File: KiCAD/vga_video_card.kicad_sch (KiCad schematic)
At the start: 16 parts, among them J1 DE15_Socket_HighDensity, J6 Conn_02x16_Odd_Even, SW1 rst_btn, SW2 SW_DPDT_x2, SW3 SW_DPDT_x2, SW4 SW_DPDT_x2, U27 74HC04, U39 74HC02, Y1 10MHz

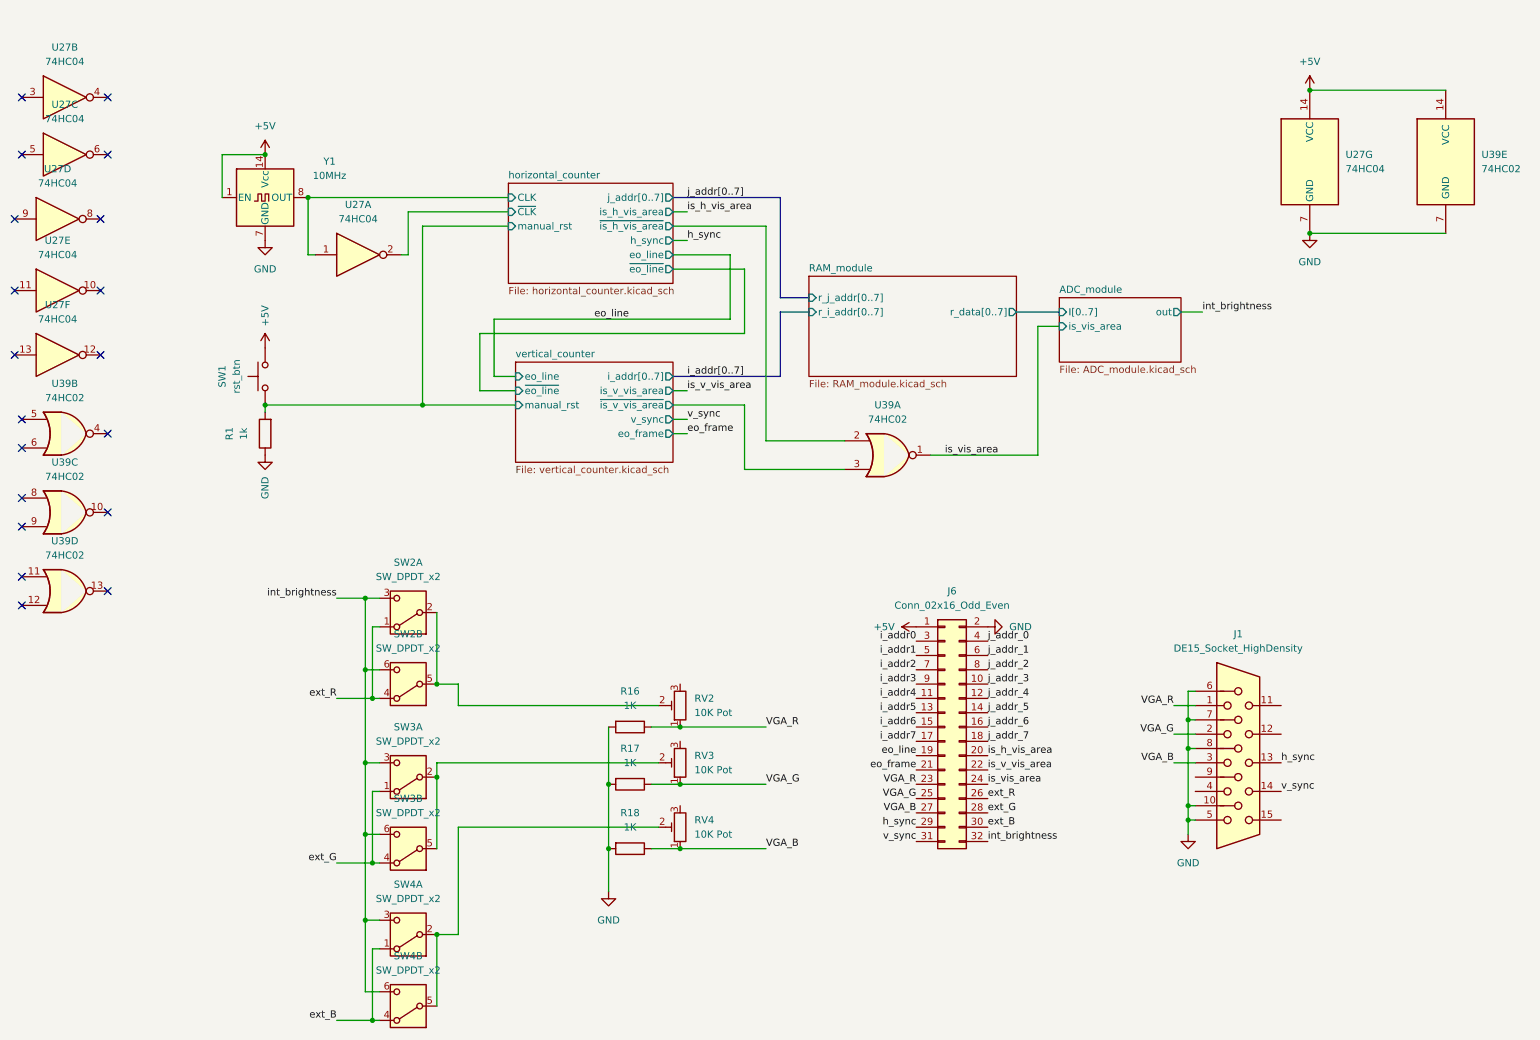
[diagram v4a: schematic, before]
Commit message: modified debug connector; changed board type in pcb editor
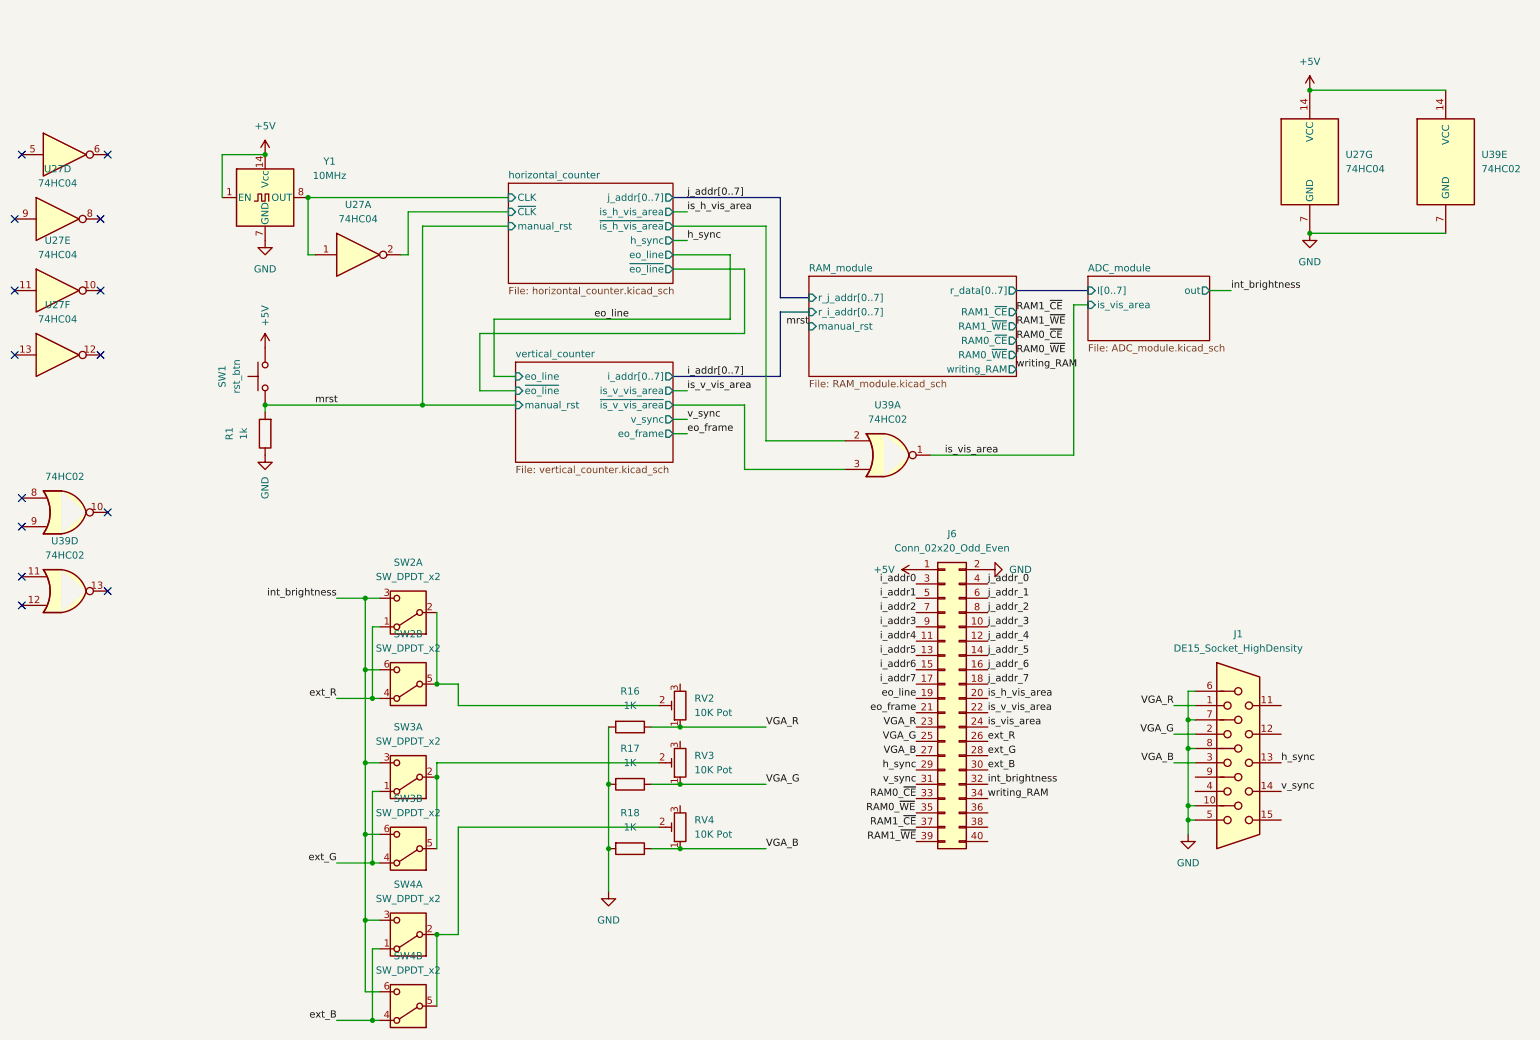
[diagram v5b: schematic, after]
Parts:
- removed J6: Conn_02x16_Odd_Even, Connector_PinSocket_2.54mm:PinSocket_2x16_P2.54mm_Vertical, symbol Connector_Generic:Conn_02x16_Odd_Even
- removed unit 2 of U27
- removed unit 2 of U39
- added J6: Conn_02x20_Odd_Even, Connector_PinSocket_2.54mm:PinSocket_2x20_P2.54mm_Vertical, symbol Connector_Generic:Conn_02x20_Odd_Even
- J1: footprint Connector_Dsub:DSUB-15_Socket_EdgeMount_P2.77mm -> Connector_Dsub:DSUB-15-HD_Socket_Horizontal_P2.29x1.90mm_EdgePinOffset3.03mm_Housed_MountingHolesOffset4.94mm
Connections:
- net +5V: now also J6.1 (Pin_1)
- net GND: now also J6.2 (Pin_2)
- net VGA_B: now also J6.27 (Pin_27)
- net VGA_G: now also J6.25 (Pin_25)
- net VGA_R: now also J6.23 (Pin_23)
- net eo_frame: now also J6.21 (Pin_21)
- net eo_line: now also J6.19 (Pin_19)
- net ext_B: now also J6.30 (Pin_30)
- net ext_G: now also J6.28 (Pin_28)
- net ext_R: now also J6.26 (Pin_26)
- net h_sync: now also J6.29 (Pin_29)
- net i_addr0: now also J6.3 (Pin_3)
- net i_addr1: now also J6.5 (Pin_5)
- net i_addr2: now also J6.7 (Pin_7)
- net i_addr3: now also J6.9 (Pin_9)
- net i_addr4: now also J6.11 (Pin_11)
- net i_addr5: now also J6.13 (Pin_13)
- net i_addr6: now also J6.15 (Pin_15)
- net i_addr7: now also J6.17 (Pin_17)
- net int_brightness: now also J6.32 (Pin_32)
- net is_h_vis_area: now also J6.20 (Pin_20)
- net is_v_vis_area: now also J6.22 (Pin_22)
- net is_vis_area: now also J6.24 (Pin_24)
- net j_addr_0: now also J6.4 (Pin_4)
- net j_addr_1: now also J6.6 (Pin_6)
- net j_addr_2: now also J6.8 (Pin_8)
- net j_addr_3: now also J6.10 (Pin_10)
- net j_addr_4: now also J6.12 (Pin_12)
- net j_addr_5: now also J6.14 (Pin_14)
- net j_addr_6: now also J6.16 (Pin_16)
- net j_addr_7: now also J6.18 (Pin_18)
- net v_sync: now also J6.31 (Pin_31)
- net horizontal_counter/manual_rst renamed mrst
- new net RAM0_~{CE}: J6.33 (Pin_33)
- new net RAM1_~{CE}: J6.37 (Pin_37)
- new net RAM1_~{WE}: J6.39 (Pin_39)
- new net writing_RAM: J6.34 (Pin_34)
- no-connect marks 19 -> 14
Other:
- sheet RAM_module ports: added RAM0_~{CE}, RAM0_~{WE}, RAM1_~{CE}, RAM1_~{WE}, manual_rst, writing_RAM; removed none

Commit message: update pcb
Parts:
- added unit 2 of U27
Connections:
- no-connect marks 14 -> 16
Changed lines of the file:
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@@
 	)
 	(no_connect
-		(at 16.51 34.29)
+		(at 15.24 31.75)
 	)
 	(no_connect
@@
 	)
 	(no_connect
+		(at 30.48 19.05)
+	)
+	(no_connect
 		(at 16.51 114.3)
 	)
 	(no_connect
-		(at 31.75 34.29)
+		(at 15.24 19.05)
+	)
+	(no_connect
+		(at 30.48 31.75)
 	)
 	(no_connect
@@
 	(symbol
 		(lib_id "74xx:74HC04")
-		(at 24.13 34.29 0)
+		(at 22.86 31.75 0)
 		(unit 3)
 		(exclude_from_sim no)
@@
 		(fields_autoplaced yes)
 		(property "Reference" "U27"
-			(at 24.13 25.4 0)
+			(at 22.86 22.86 0)
 			(effects
 				(font
 					(size 1.27 1.27)
 				)
-				(hide yes)
 			)
 		)
 		(property "Value" "74HC04"
-			(at 24.13 27.94 0)
+			(at 22.86 25.4 0)
 			(effects
 				(font
 					(size 1.27 1.27)
 				)
-				(hide yes)
 			)
 		)
 		(property "Footprint" "Package_DIP:DIP-14_W7.62mm"
-			(at 24.13 34.29 0)
+			(at 22.86 31.75 0)
 			(effects
 				(font
@@
 		)
 		(property "Datasheet" "https://assets.nexperia.com/documents/data-sheet/74HC_HCT04.pdf"
-			(at 24.13 34.29 0)
+			(at 22.86 31.75 0)
 			(effects
 				(font
@@
 		)
 		(property "Description" "Hex Inverter"
-			(at 24.13 34.29 0)
+			(at 22.86 31.75 0)
 			(effects
 				(font
@@
 				)
 			)
+		)
+	)
+	(symbol
+		(lib_id "74xx:74HC04")
+		(at 22.86 19.05 0)
+		(unit 2)
+		(exclude_from_sim no)
+		(in_bom yes)
+		(on_board yes)
+		(dnp no)
+		(fields_autoplaced yes)
+		(property "Reference" "U27"
+			(at 22.86 10.16 0)
+			(effects
+				(font
+					(size 1.27 1.27)
+				)
+			)
+		)
+		(property "Value" "74HC04"
+			(at 22.86 12.7 0)
+			(effects
+				(font
+					(size 1.27 1.27)
+				)
+			)
+		)
+		(property "Footprint" "Package_DIP:DIP-14_W7.62mm"
+			(at 22.86 19.05 0)
+			(effects
+				(font
+					(size 1.27 1.27)
+				)
+				(hide yes)
+			)
+		)
+		(property "Datasheet" "https://assets.nexperia.com/documents/data-sheet/74HC_HCT04.pdf"
+			(at 22.86 19.05 0)
+			(effects
+				(font
+					(size 1.27 1.27)
+				)
+				(hide yes)
+			)
+		)
+		(property "Description" "Hex Inverter"
+			(at 22.86 19.05 0)
+			(effects
+				(font
+					(size 1.27 1.27)
+				)
+				(hide yes)
+			)
+		)
+		(pin "14"
+		)
+		(pin "3"
+		)
+		(pin "10"
+		)
+		(pin "1"
+		)
+		(pin "5"
+		)
+		(pin "11"
+		)
+		(pin "12"
+		)
+		(pin "4"
+		)
+		(pin "7"
+		)
+		(pin "9"
+		)
+		(pin "8"
+		)
+		(pin "13"
+		)
+		(pin "2"
+		)
+		(pin "6"
+		)
+		(instances
+			(project "vga_video_card"
+				(path "/53ebbfbe-eaa1-4706-acc1-611a99db7179"
+					(reference "U27")
+					(unit 2)
+				)
+			)

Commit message: fix multiple ERCs that made RAM addrs not connecting
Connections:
- net RAM0_~{WE}: now also J6.35 (Pin_35)
- net j_addr_0 renamed j_addr0
- net j_addr_1 renamed j_addr1
- net j_addr_2 renamed j_addr2
- net j_addr_3 renamed j_addr3
- net j_addr_4 renamed j_addr4
- net j_addr_5 renamed j_addr5
- net j_addr_6 renamed j_addr6
- net j_addr_7 renamed j_addr7
- no-connect marks 16 -> 27
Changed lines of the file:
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@@
+	)
+	(no_connect
+		(at 133.35 149.86)
 	)
 	(no_connect
@@
 	)
 	(no_connect
+		(at 224.79 147.32)
+	)
+	(no_connect
 		(at 15.24 45.72)
 	)
 	(no_connect
+		(at 187.96 151.13)
+	)
+	(no_connect
 		(at 16.51 109.22)
 	)
@@
 	)
 	(no_connect
+		(at 240.03 137.16)
+	)
+	(no_connect
 		(at 30.48 45.72)
 	)
 	(no_connect
+		(at 187.96 153.67)
+	)
+	(no_connect
 		(at 15.24 58.42)
 	)
@@
 	)
 	(no_connect
+		(at 240.03 152.4)
+	)
+	(no_connect
+		(at 187.96 156.21)
+	)
+	(no_connect
 		(at 30.48 19.05)
 	)
@@
 	)
 	(no_connect
+		(at 133.35 138.43)
+	)
+	(no_connect
 		(at 30.48 31.75)
 	)
 	(no_connect
+		(at 133.35 128.27)
+	)
+	(no_connect
 		(at 30.48 58.42)
 	)
+	(no_connect
+		(at 224.79 144.78)
+	)
+	(no_connect
+		(at 240.03 132.08)
+	)
 	(wire
 		(pts
@@
 			(width 0)
 			(type default)
+		)
+	)
+	(label "j_addr3"
+		(at 187.96 118.11 0)
+		(effects
+			(font
+				(size 1.27 1.27)
+			)
+			(justify left bottom)
 		)
 	)
@@
 		)
 	)
-	(label "j_addr_2"
-		(at 187.96 115.57 0)
-		(effects
-			(font
-				(size 1.27 1.27)
-			)
-			(justify left bottom)
-		)
-	)
 	(label "v_sync"
 		(at 175.26 146.05 180)
@@
 		)
 	)
+	(label "j_addr0"
+		(at 187.96 110.49 0)
+		(effects
+			(font
+				(size 1.27 1.27)
+			)
+			(justify left bottom)
+		)
+	)
 	(label "VGA_R"
 		(at 148.59 135.89 0)
@@
 		)
 	)
-	(label "j_addr_0"
-		(at 187.96 110.49 0)
-		(effects
-			(font
-				(size 1.27 1.27)
-			)
-			(justify left bottom)
-		)
-	)
 	(label "VGA_B"
 		(at 148.59 157.48 0)
@@
 		)
 	)
-	(label "j_addr_7"
-		(at 187.96 128.27 0)
-		(effects
-			(font
-				(size 1.27 1.27)
-			)
-			(justify left bottom)
-		)
-	)
 	(label "RAM0_~{CE}"
 		(at 175.26 148.59 180)
@@
 		)
 	)
-	(label "j_addr_3"
-		(at 187.96 118.11 0)
+	(label "j_addr1"
+		(at 187.96 113.03 0)
 		(effects
 			(font
@@
 		)
 	)
-	(label "j_addr_6"
-		(at 187.96 125.73 0)
-		(effects
-			(font
-				(size 1.27 1.27)
-			)
-			(justify left bottom)
-		)
-	)
 	(label "is_v_vis_area"
 		(at 187.96 133.35 0)
@@
 		)
 	)
+	(label "j_addr7"
+		(at 187.96 128.27 0)
+		(effects
+			(font
+				(size 1.27 1.27)
+			)
+			(justify left bottom)
+		)
+	)
+	(label "j_addr6"
+		(at 187.96 125.73 0)
+		(effects
+			(font
+				(size 1.27 1.27)
+			)
+			(justify left bottom)
+		)
+	)
 	(label "eo_frame"
 		(at 175.26 133.35 180)
@@
 		)
 	)
+	(label "j_addr2"
+		(at 187.96 115.57 0)
+		(effects
+			(font
+				(size 1.27 1.27)
+			)
+			(justify left bottom)
+		)
+	)
 	(label "is_vis_area"
 		(at 187.96 135.89 0)
@@
 		)
 	)
+	(label "j_addr4"
+		(at 187.96 120.65 0)
+		(effects
+			(font
+				(size 1.27 1.27)
+			)
+			(justify left bottom)
+		)
+	)
 	(label "i_addr6"
 		(at 175.26 125.73 180)
@@
 		)
 	)
-	(label "j_addr_1"
-		(at 187.96 113.03 0)
-		(effects
-			(font
-				(size 1.27 1.27)
-			)
-			(justify left bottom)
-		)
-	)
 	(label "RAM1_~{CE}"
 		(at 193.04 62.23 0)
@@
 	)
 	(label "RAM0_~{WE}"
-		(at 166.37 151.13 0)
-		(effects
-			(font
-				(size 1.27 1.27)
-			)
-			(justify left bottom)
+		(at 175.26 151.13 180)
+		(effects
+			(font
+				(size 1.27 1.27)
+			)
+			(justify right bottom)
 		)
 	)
@@
 		)
 	)
-	(label "j_addr_5"
-		(at 187.96 123.19 0)
-		(effects
-			(font
-				(size 1.27 1.27)
-			)
-			(justify left bottom)
-		)
-	)
 	(label "ext_B"
 		(at 187.96 143.51 0)
@@
 		)
 	)
+	(label "j_addr5"
+		(at 187.96 123.19 0)
+		(effects
+			(font
+				(size 1.27 1.27)
+			)
+			(justify left bottom)
+		)
+	)
 	(label "h_sync"
 		(at 175.26 143.51 180)
@@
 		(effects
 			(font
-				(size 1.27 1.27)
-			)
-			(justify left bottom)
-		)
-	)
-	(label "j_addr_4"
-		(at 187.96 120.65 0)
-		(effects
-			(font

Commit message: resolve ERCs for addr combiner
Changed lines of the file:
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@@
 	(paper "A4")
+	(junction
+		(at 175.26 107.95)
+		(diameter 0)
+		(color 0 0 0 0)
+	)
 	(junction
 		(at 133.35 146.05)
@@
 	)
 	(junction
+		(at 187.96 107.95)
+		(diameter 0)
+		(color 0 0 0 0)
+	)
+	(junction
 		(at 77.47 113.03)
 		(diameter 0)
@@
 	(wire
 		(pts
+			(xy 154.94 64.77) (xy 156.21 64.77)
+		)
+		(stroke
+			(width 0)
+			(type default)
+		)
+	)
+	(wire
+		(pts
 			(xy 132.08 78.74) (xy 144.78 78.74)
 		)
@@
 	(wire
 		(pts
+			(xy 187.96 101.6) (xy 187.96 107.95)
+		)
+		(stroke
+			(width 0)
+			(type default)
+		)
+	)
+	(wire
+		(pts
 			(xy 90.17 144.78) (xy 90.17 157.48)
 		)
@@
 		(pts
 			(xy 72.39 187.96) (xy 78.74 187.96)
+		)
+		(stroke
+			(width 0)
+			(type default)
+		)
+	)
+	(wire
+		(pts
+			(xy 175.26 101.6) (xy 175.26 107.95)
 		)
 		(stroke
@@
 	)
 	(label "mrst"
-		(at 156.21 64.77 180)
+		(at 154.94 64.77 270)
 		(effects
 			(font
@@
 	)
 	(symbol
+		(lib_id "power:PWR_FLAG")
+		(at 187.96 101.6 0)
+		(mirror y)
+		(unit 1)
+		(exclude_from_sim no)
+		(in_bom yes)
+		(on_board yes)
+		(dnp no)
+		(property "Reference" "#FLG02"
+			(at 187.96 99.695 0)
+			(effects
+				(font
+					(size 1.27 1.27)
+				)
+				(hide yes)
+			)
+		)
+		(property "Value" "PWR_FLAG"
+			(at 187.96 96.52 0)
+			(effects
+				(font
+					(size 1.27 1.27)
+				)
+			)
+		)
+		(property "Footprint" ""
+			(at 187.96 101.6 0)
+			(effects
+				(font
+					(size 1.27 1.27)
+				)
+				(hide yes)
+			)
+		)
+		(property "Datasheet" "~"
+			(at 187.96 101.6 0)
+			(effects
+				(font
+					(size 1.27 1.27)
+				)
+				(hide yes)
+			)
+		)
+		(property "Description" "Special symbol for telling ERC where power comes from"
+			(at 187.96 101.6 0)
+			(effects
+				(font
+					(size 1.27 1.27)
+				)
+				(hide yes)
+			)
+		)
+		(pin "1"
+		)
+		(instances
+			(project ""
+				(path "/53ebbfbe-eaa1-4706-acc1-611a99db7179"
+					(reference "#FLG02")
+					(unit 1)
+				)
+			)
+		)
+	)
+	(symbol
 		(lib_id "Switch:SW_DPDT_x2")
 		(at 85.09 128.27 180)
@@
 					(unit 1)
 				)
+			)
+		)
+	)
+	(symbol
+		(lib_id "power:PWR_FLAG")
+		(at 175.26 101.6 0)
+		(unit 1)
+		(exclude_from_sim no)
+		(in_bom yes)
+		(on_board yes)
+		(dnp no)
+		(fields_autoplaced yes)
+		(property "Reference" "#FLG01"
+			(at 175.26 99.695 0)
+			(effects
+				(font
+					(size 1.27 1.27)
+				)
+				(hide yes)
+			)
+		)
+		(property "Value" "PWR_FLAG"
+			(at 175.26 96.52 0)
+			(effects
+				(font
+					(size 1.27 1.27)
+				)
+			)
+		)
+		(property "Footprint" ""
+			(at 175.26 101.6 0)
+			(effects
+				(font
+					(size 1.27 1.27)
+				)
+				(hide yes)
+			)
+		)
+		(property "Datasheet" "~"
+			(at 175.26 101.6 0)
+			(effects
+				(font
+					(size 1.27 1.27)
+				)
+				(hide yes)
+			)
+		)
+		(property "Description" "Special symbol for telling ERC where power comes from"
+			(at 175.26 101.6 0)
+			(effects
+				(font
+					(size 1.27 1.27)
+				)
+				(hide yes)
+			)
+		)
+		(pin "1"
+		)
+		(instances
+			(project ""
+				(path "/53ebbfbe-eaa1-4706-acc1-611a99db7179"
+					(reference "#FLG01")
+					(unit 1)
+				)
